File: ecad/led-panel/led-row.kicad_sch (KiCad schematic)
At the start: 9 parts

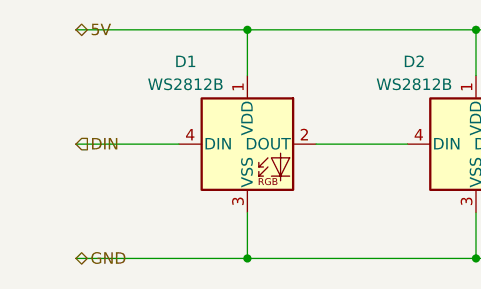
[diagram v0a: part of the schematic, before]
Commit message: added vertical USB-C connector to controller board; and possibly much more
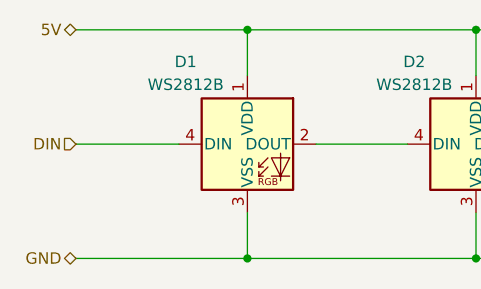
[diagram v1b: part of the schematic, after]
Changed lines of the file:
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@@
 	(hierarchical_label "5V"
 		(shape bidirectional)
-		(at 25.4 31.75 0)
+		(at 25.4 31.75 180)
 		(effects
 			(font
 				(size 1.27 1.27)
 			)
-			(justify left)
+			(justify right)
 		)
 	)
 	(hierarchical_label "DIN"
 		(shape input)
-		(at 25.4 44.45 0)
+		(at 25.4 44.45 180)
 		(effects
 			(font
 				(size 1.27 1.27)
 			)
-			(justify left)
+			(justify right)
 		)
 	)
@@
 	(hierarchical_label "GND"
 		(shape bidirectional)
-		(at 25.4 57.15 0)
+		(at 25.4 57.15 180)
 		(effects
 			(font
 				(size 1.27 1.27)
 			)
-			(justify left)
+			(justify right)
 		)
 	)

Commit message: populate BOM fields with MPN and LCSC Part #
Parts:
- D1, D2, D3, D4, D5, D6, D7, D8, D9: LCSC# (none) -> C2874885; MPN (none) -> WS2812B-V5/W
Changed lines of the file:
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@@
+			)
+		)
+		(property "LCSC#" "C2874885"
+			(at 44.45 44.45 0)
+			(hide yes)
+			(show_name no)
+			(do_not_autoplace no)
+			(effects
+				(font
+					(size 1.27 1.27)
+				)
+			)
+		)
+		(property "MPN" "WS2812B-V5/W"
+			(at 44.45 44.45 0)
+			(hide yes)
+			(show_name no)
+			(do_not_autoplace no)
+			(effects
+				(font
+					(size 1.27 1.27)
+				)
 			)
 		)
@@
 			)
 		)
+		(property "LCSC#" "C2874885"
+			(at 146.05 44.45 0)
+			(hide yes)
+			(show_name no)
+			(do_not_autoplace no)
+			(effects
+				(font
+					(size 1.27 1.27)
+				)
+			)
+		)
+		(property "MPN" "WS2812B-V5/W"
+			(at 146.05 44.45 0)
+			(hide yes)
+			(show_name no)
+			(do_not_autoplace no)
+			(effects
+				(font
+					(size 1.27 1.27)
+				)
+			)
+		)
 		(pin "2"
 		)
@@
 			)
 		)
+		(property "LCSC#" "C2874885"
+			(at 171.45 44.45 0)
+			(hide yes)
+			(show_name no)
+			(do_not_autoplace no)
+			(effects
+				(font
+					(size 1.27 1.27)
+				)
+			)
+		)
+		(property "MPN" "WS2812B-V5/W"
+			(at 171.45 44.45 0)
+			(hide yes)
+			(show_name no)
+			(do_not_autoplace no)
+			(effects
+				(font
+					(size 1.27 1.27)
+				)
+			)
+		)
 		(pin "2"
 		)
@@
 			)
 		)
+		(property "LCSC#" "C2874885"
+			(at 222.25 44.45 0)
+			(hide yes)
+			(show_name no)
+			(do_not_autoplace no)
+			(effects
+				(font
+					(size 1.27 1.27)
+				)
+			)
+		)
+		(property "MPN" "WS2812B-V5/W"
+			(at 222.25 44.45 0)
+			(hide yes)
+			(show_name no)
+			(do_not_autoplace no)
+			(effects
+				(font
+					(size 1.27 1.27)
+				)
+			)
+		)
 		(pin "2"
 		)
@@
 			)
 		)
+		(property "LCSC#" "C2874885"
+			(at 196.85 44.45 0)
+			(hide yes)
+			(show_name no)
+			(do_not_autoplace no)
+			(effects
+				(font
+					(size 1.27 1.27)
+				)
+			)
+		)
+		(property "MPN" "WS2812B-V5/W"
+			(at 196.85 44.45 0)
+			(hide yes)
+			(show_name no)
+			(do_not_autoplace no)
+			(effects
+				(font
+					(size 1.27 1.27)
+				)
+			)
+		)
 		(pin "2"
 		)
@@
 			)
 		)
+		(property "LCSC#" "C2874885"
+			(at 95.25 44.45 0)
+			(hide yes)
+			(show_name no)
+			(do_not_autoplace no)
+			(effects
+				(font
+					(size 1.27 1.27)
+				)
+			)
+		)
+		(property "MPN" "WS2812B-V5/W"
+			(at 95.25 44.45 0)
+			(hide yes)
+			(show_name no)
+			(do_not_autoplace no)
+			(effects
+				(font
+					(size 1.27 1.27)
+				)
+			)
+		)
 		(pin "2"
 		)
@@
 			)
 		)
+		(property "LCSC#" "C2874885"
+			(at 120.65 44.45 0)
+			(hide yes)
+			(show_name no)
+			(do_not_autoplace no)
+			(effects
+				(font
+					(size 1.27 1.27)
+				)
+			)
+		)
+		(property "MPN" "WS2812B-V5/W"
+			(at 120.65 44.45 0)
+			(hide yes)
+			(show_name no)
+			(do_not_autoplace no)
+			(effects
+				(font
+					(size 1.27 1.27)
+				)
+			)
+		)
 		(pin "2"
 		)
@@
 			)
 		)
+		(property "LCSC#" "C2874885"
+			(at 247.65 44.45 0)
+			(hide yes)
+			(show_name no)
+			(do_not_autoplace no)
+			(effects
+				(font
+					(size 1.27 1.27)
+				)
+			)
+		)
+		(property "MPN" "WS2812B-V5/W"
+			(at 247.65 44.45 0)
+			(hide yes)
+			(show_name no)
+			(do_not_autoplace no)
+			(effects
+				(font
+					(size 1.27 1.27)
+				)
+			)
+		)
 		(pin "2"
 		)
@@
 			(at 69.85 44.45 0)
 			(hide yes)
+			(show_name no)
+			(do_not_autoplace no)
+			(effects
+				(font
+					(size 1.27 1.27)
+				)
+			)
+		)
+		(property "LCSC#" "C2874885"
+			(at 69.85 44.45 0)
+			(hide yes)
+			(show_name no)
+			(do_not_autoplace no)
+			(effects
+				(font
+					(size 1.27 1.27)
+				)
+			)
+		)
+		(property "MPN" "WS2812B-V5/W"
+			(at 69.85 44.45 0)
+			(hide yes)
